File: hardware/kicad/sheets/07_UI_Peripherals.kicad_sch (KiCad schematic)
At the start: 0 parts

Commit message: Implement ESP32-S3 core subsystem
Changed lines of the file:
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@@
-    (effects (font (size 1.27 1.27)) (justify left))
-  )
-  (hierarchical_label "RGB_R_MCU" (shape input) (at 25.4 80.56 0)
-    (effects (font (size 1.27 1.27)) (justify left))
-  )
-  (hierarchical_label "RGB_G_MCU" (shape input) (at 25.4 85.64 0)
-    (effects (font (size 1.27 1.27)) (justify left))
-  )
-  (hierarchical_label "RGB_B_MCU" (shape input) (at 25.4 90.72 0)
-    (effects (font (size 1.27 1.27)) (justify left))
-  )
-  (hierarchical_label "BUZZER_OUT_MCU" (shape input) (at 25.4 95.80 0)
-    (effects (font (size 1.27 1.27)) (justify left))
-  )
-  (hierarchical_label "OLED_RESET_MCU" (shape input) (at 25.4 100.88 0)
     (effects (font (size 1.27 1.27)) (justify left))
   )

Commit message: Implement Package 08 local user interface
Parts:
- added C1: 100 nF X7R ±10% expander reset delay, symbol IPC100:C
- added Q1: 2N7002-class open-drain reset; 100k core pull-up 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, symbol IPC100:OLED_RESET_OD
- added R1: 100 kΩ ±1% expander reset pull-up, symbol IPC100:R
- added R2: 4.70 kΩ ±1% I2C SDA pull-up; Sheet 07 base-bus ow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, symbol IPC100:R
- added R3: 4.70 kΩ ±1% I2C SCL pull-up; Sheet 07 base-bus ow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, symbol IPC100:R
- added TP1: UI_VCC DFT node, symbol IPC100:TEST_NODE
- added TP2: OLED_VCC DFT node, symbol IPC100:TEST_NODE
- added TP3: I2C_SDA DFT node, symbol IPC100:TEST_NODE
- added TP4: I2C_SCL DFT node, symbol IPC100:TEST_NODE
- added TP5: ENCODER_A_COND DFT node, symbol IPC100:TEST_NODE
- added U1: 3ch active-low panel encoder conditioner; 10k/1k/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, symbol IPC100:ENCODER_CONDITIONER3
- added U2: TCA9535-class, +3V3_CORE, address 0x20, power-up 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, symbol IPC100:I2C_EXPANDER
- added U3: 4x 60 V logic NMOS; 100Ω gates; 100kΩ gate pull-d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, symbol IPC100:STATUS_DRIVER4
- added U4: 2.42-inch SSD1309 OLED reference; exact module/J6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, symbol IPC100:I2C_PERIPHERAL_BOUNDARY
- added U5: BME280 environmental sensor reference; exact modu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, symbol IPC100:I2C_PERIPHERAL_BOUNDARY
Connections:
- net +3V3_CORE: now also Q1.1 (RELEASE_CTL), R1.2, R2.2, R3.2, U1.6 (GND), U2.6 (GND)
- net BUZZER_OUT: now also U3.6 (RGB_R)
- net ENCODER_A_COND: now also TP5.1 (NODE), U1.9 (SW_COND)
- net ENCODER_A_RAW: now also U1.4 (B_RAW)
- net ENCODER_B_COND: now also U1.8 (B_COND)
- net ENCODER_B_RAW: now also U1.3 (A_RAW)
- net ENCODER_SW_COND: now also U1.7 (A_COND)
- net ENCODER_SW_RAW: now also U1.2 (UI_VCC)
- net I2C_SCL: now also R3.1, TP4.1 (NODE), U2.5 (ADDR), U4.2 (SDA), U5.2 (SDA)
- net I2C_SDA: now also R2.1, TP3.1 (NODE), U4.3 (SCL), U5.3 (SCL)
- net OLED_RESET: now also Q1.4 (OLED_RESET), U4.1 (VCC)
- net OLED_VCC: now also TP2.1 (NODE), U4.4 (RESET_OR_NC)
- net RGB_B: now also U3.7 (RGB_G)
- net RGB_G: now also U3.8 (RGB_B)
- net RGB_R: now also U3.9 (BUZZER_OUT)
- net SENSOR_VCC: now also U5.4 (RESET_OR_NC)
- net UI_VCC: now also TP1.1 (NODE), U1.5 (SW_RAW)
- new net BUZZER_CTL: U2.8 (RGB_G_CTL), U3.1 (R_CTL)
- new net GND: C1.1, U1.1 (3V3), U2.1 (VCC), U2.3 (SCL)
- new net OLED_RESET_RELEASE: Q1.2 (3V3_DEFAULT_ASSERT), U2.7 (RGB_R_CTL)
- new net RGB_B_CTL: U2.9 (RGB_B_CTL), U3.2 (G_CTL)
- new net RGB_G_CTL: U2.10 (BUZZER_CTL), U3.3 (B_CTL)
- new net RGB_R_CTL: U2.11 (OLED_RESET_RELEASE), U3.4 (BUZ_CTL)
- new net UI_EXPANDER_RESET_N: C1.2, R1.1, U2.4 (RESET_N)
- no-connect marks 0 -> 1
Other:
- note added: "1 — PANEL ENCODER CONDITIONING (ORDINARY UI REQUESTS; NOT SAFETY AUTHORITY)"
- note added: "2 — CORE-POWERED I2C EXPANDER / SAFE-DEFAULT STATUS CONTROL"
- note added: "3 — MAIN-ONLY RGB / BUZZER LOW-SIDE DRIVERS"
- note added: "4 — OLED RESET / DISPLAY & SENSOR I2C BOUNDARIES"
- note added: "5 — SCHEMATIC DFT NODES (PHYSICAL PADS OWNED BY SHEET 09 / PCB DFT)"
- note added: "6 — HIERARCHICAL FUNCTIONAL INTERFACES"
- note added: "Each channel: 10 kΩ UI-domain bias, 1 kΩ series protection, 10 nF filter, Schmitt receiver, low-capacitance ESD provision. UI_VCC invalid forces conditioned output inactive low. Firmware debounce remains required."
- note added: "No ARM/FIRE/STOP, analog adjustment, motor, relay, watchdog, authorization, connector, or raw GPIO circuitry exists on Sheet 07. GPIO37 remains reserved; GPIO42 remains WATCHDOG_SERVICE_MCU on Sheet 03."
- note added: "OLED/SENSOR rails are switched only by Sheet 02 from Sheet 03 requests. Sheet 07 adds no power switch. I2C pull-ups remain core-powered; exact modules must be unpowered-bus safe or receive series isolation in their released interface."
- note added: "Outputs are open-drain current sinks for later Sheet 09 loads. RGB current resistors and final buzzer device remain connector/load dependent; U3 provides only drive, default-OFF bias, and magnetic-load clamp provision."
- note added: "Panel ESD devices and physical connector pinout remain Sheet 09 work. Sheet 07 defines electrical ESD/series/filter requirements only. All component classes and values are preliminary; all footprints remain blank."
- note removed: "Detailed implementation intentionally deferred to subsequent engineering package."
- note removed: "PACKAGE 01 PLACEHOLDER — NO CIRCUITRY OR FOOTPRINTS"
- title: IPC-100 Rev A — 07 UI + OLED + Sensor -> IPC-100 Rev A — 07 User Interface & Local Controls

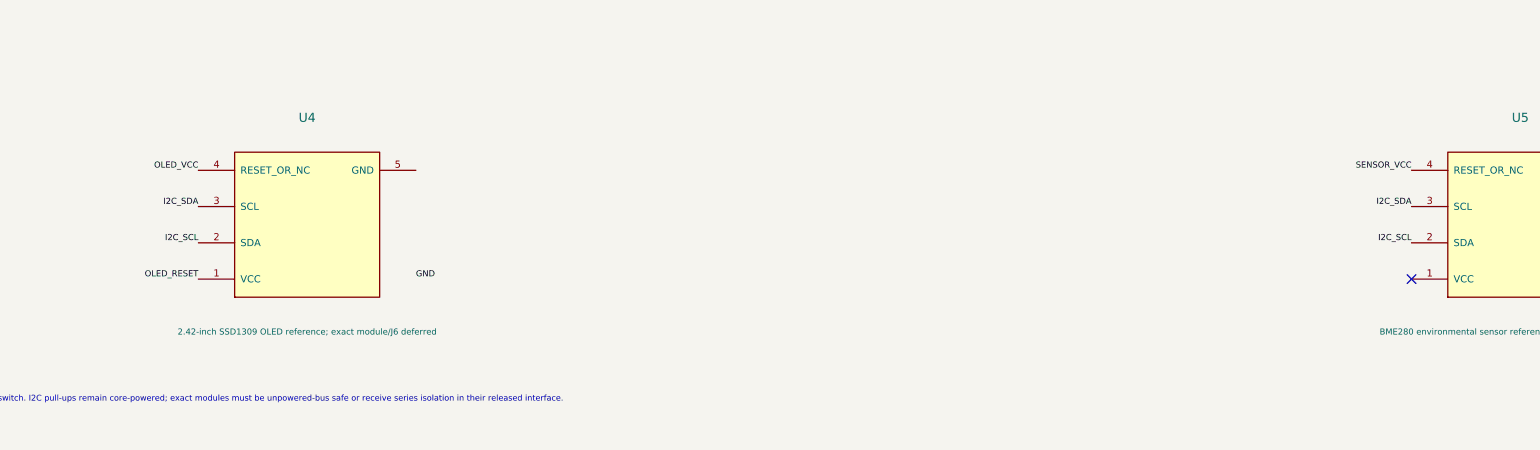
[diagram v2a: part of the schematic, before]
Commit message: Complete ECO-003 hierarchy exposure
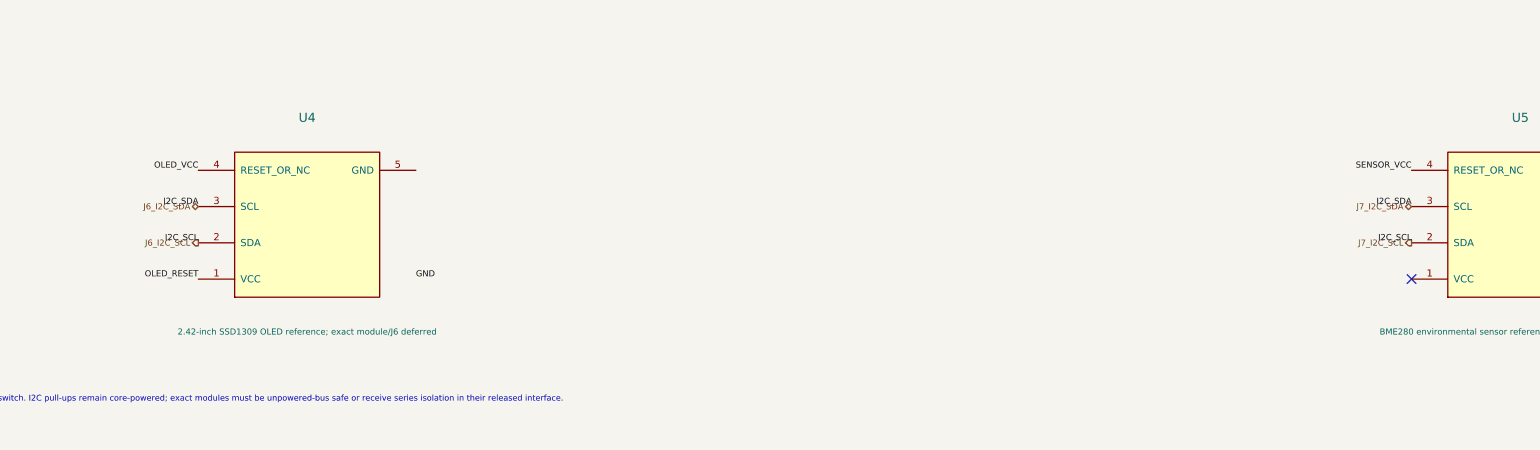
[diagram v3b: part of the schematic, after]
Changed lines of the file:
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@@
   (label "I2C_SDA" (at 104.76 152.46 180) (effects (font (size 0.85 0.85)) (justify right bottom)))
   (label "I2C_SCL" (at 104.76 157.54 180) (effects (font (size 0.85 0.85)) (justify right bottom)))
+  (hierarchical_label "J6_I2C_SDA" (shape bidirectional) (at 104.76 152.46 180) (effects (font (size 0.85 0.85)) (justify right)))
+  (hierarchical_label "J6_I2C_SCL" (shape output) (at 104.76 157.54 180) (effects (font (size 0.85 0.85)) (justify right)))
   (label "OLED_RESET" (at 104.76 162.62 180) (effects (font (size 0.85 0.85)) (justify right bottom)))
   (label "GND" (at 135.24 162.62 0) (effects (font (size 0.85 0.85)) (justify left bottom)))
@@
   (label "I2C_SDA" (at 274.76 152.46 180) (effects (font (size 0.85 0.85)) (justify right bottom)))
   (label "I2C_SCL" (at 274.76 157.54 180) (effects (font (size 0.85 0.85)) (justify right bottom)))
+  (hierarchical_label "J7_I2C_SDA" (shape bidirectional) (at 274.76 152.46 180) (effects (font (size 0.85 0.85)) (justify right)))
+  (hierarchical_label "J7_I2C_SCL" (shape output) (at 274.76 157.54 180) (effects (font (size 0.85 0.85)) (justify right)))
   (no_connect (at 274.76 162.62))
   (label "GND" (at 305.24 162.62 0) (effects (font (size 0.85 0.85)) (justify left bottom)))

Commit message: Complete ECO-004 interface remediation
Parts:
- added U6: J6: 100 kHz; OLED_VCC-qualified; fail-disabled; I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, symbol IPC100:I2C_POWER_QUALIFIED_BRANCH
- added U7: J7: 100 kHz; SENSOR_VCC-qualified; fail-disabled;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, symbol IPC100:I2C_POWER_QUALIFIED_BRANCH
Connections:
- net +3V3_CORE: now also U6.4 (GND), U7.4 (GND)
- net GND: now also U6.1 (BASE_VDD), U6.5 (BRANCH_VDD_QUAL), U7.1 (BASE_VDD), U7.5 (BRANCH_VDD_QUAL)
- net I2C_SCL: now also U6.3 (SCL_BASE), U7.3 (SCL_BASE); no longer U4.2 (SDA), U5.2 (SDA)
- net I2C_SDA: no longer U4.3 (SCL), U5.3 (SCL)
- net OLED_VCC: now also U6.8 (GND)
- net SENSOR_VCC: now also U7.8 (GND)
- new net J6_I2C_SCL: U4.2 (SDA), U6.7 (SCL_BRANCH)
- new net J6_I2C_SDA: U4.3 (SCL)
- new net J7_I2C_SCL: U5.2 (SDA), U7.7 (SCL_BRANCH)
- new net J7_I2C_SDA: U5.3 (SCL)
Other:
- note added: "OLED/SENSOR rails remain Sheet 02 controlled. U6/U7 qualify directly from their own branch rail and isolate before it is invalid. Sheet 07 remains sole owner of the 4.70k base-bus pull-up pair; no branch or Sheet 09 pull-ups."
- note removed: "OLED/SENSOR rails are switched only by Sheet 02 from Sheet 03 requests. Sheet 07 adds no power switch. I2C pull-ups remain core-powered; exact modules must be unpowered-bus safe or receive series isolation in their released interface."
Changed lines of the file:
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@@
   )
   (label "OLED_VCC" (at 104.76 147.38 180) (effects (font (size 0.85 0.85)) (justify right bottom)))
-  (label "I2C_SDA" (at 104.76 152.46 180) (effects (font (size 0.85 0.85)) (justify right bottom)))
-  (label "I2C_SCL" (at 104.76 157.54 180) (effects (font (size 0.85 0.85)) (justify right bottom)))
+  (label "J6_I2C_SDA" (at 104.76 152.46 180) (effects (font (size 0.85 0.85)) (justify right bottom)))
+  (label "J6_I2C_SCL" (at 104.76 157.54 180) (effects (font (size 0.85 0.85)) (justify right bottom)))
   (hierarchical_label "J6_I2C_SDA" (shape bidirectional) (at 104.76 152.46 180) (effects (font (size 0.85 0.85)) (justify right)))
   (hierarchical_label "J6_I2C_SCL" (shape output) (at 104.76 157.54 180) (effects (font (size 0.85 0.85)) (justify right)))
@@
   )
   (label "SENSOR_VCC" (at 274.76 147.38 180) (effects (font (size 0.85 0.85)) (justify right bottom)))
-  (label "I2C_SDA" (at 274.76 152.46 180) (effects (font (size 0.85 0.85)) (justify right bottom)))
-  (label "I2C_SCL" (at 274.76 157.54 180) (effects (font (size 0.85 0.85)) (justify right bottom)))
+  (label "J7_I2C_SDA" (at 274.76 152.46 180) (effects (font (size 0.85 0.85)) (justify right bottom)))
+  (label "J7_I2C_SCL" (at 274.76 157.54 180) (effects (font (size 0.85 0.85)) (justify right bottom)))
   (hierarchical_label "J7_I2C_SDA" (shape bidirectional) (at 274.76 152.46 180) (effects (font (size 0.85 0.85)) (justify right)))
   (hierarchical_label "J7_I2C_SCL" (shape output) (at 274.76 157.54 180) (effects (font (size 0.85 0.85)) (justify right)))
   (no_connect (at 274.76 162.62))
   (label "GND" (at 305.24 162.62 0) (effects (font (size 0.85 0.85)) (justify left bottom)))
-  (text "OLED/SENSOR rails are switched only by Sheet 02 from Sheet 03 requests. Sheet 07 adds no power switch. I2C pull-ups remain core-powered; exact modules must be unpowered-bus safe or receive series isolation in their released interface." (at 20 180 0) (effects (font (size 0.82 0.82)) (justify left bottom)))
+  (symbol (lib_id "IPC100:I2C_POWER_QUALIFIED_BRANCH") (at 380 150 0) (unit 1) (exclude_from_sim no) (in_bom yes) (on_board yes) (dnp no)
+    (property "Reference" "U6" (at 380 133 0) (effects (font (size 1.1 1.1))))
+    (property "Value" "J6: 100 kHz; OLED_VCC-qualified; fail-disabled; Ioff <=10uA; no backfeed/stuck-low propagation while isolated" (at 380 167 0) (effects (font (size 0.72 0.72))))
+    (property "Footprint" "" (at 380 150 0) (effects (font (size 1 1)) hide)) (property "Datasheet" "" (at 380 150 0) (effects (font (size 1 1)) hide))
+    (pin "1") (pin "2") (pin "3") (pin "4") (pin "5") (pin "6") (pin "7") (pin "8")
+    (instances (project "IPC-100" (path "/10000000-0000-4000-8000-000000000001/10000000-0000-4000-8000-000000000365" (reference "U6") (unit 1))))
+  )
+  (label "+3V3_CORE" (at 362.22 139.84 180) (effects (font (size .72 .72)) (justify right bottom)))
+  (label "I2C_SDA" (at 362.22 144.92 180) (effects (font (size .72 .72)) (justify right bottom)))
+  (label "I2C_SCL" (at 362.22 150 180) (effects (font (size .72 .72)) (justify right bottom)))
+  (label "GND" (at 362.22 160.16 180) (effects (font (size .72 .72)) (justify right bottom)))
+  (label "OLED_VCC" (at 397.78 139.84 0) (effects (font (size .72 .72)) (justify left bottom)))
+  (label "J6_I2C_SDA" (at 397.78 144.92 0) (effects (font (size .72 .72)) (justify left bottom)))
+  (label "J6_I2C_SCL" (at 397.78 150 0) (effects (font (size .72 .72)) (justify left bottom)))
+  (label "GND" (at 397.78 160.16 0) (effects (font (size .72 .72)) (justify left bottom)))
+  (symbol (lib_id "IPC100:I2C_POWER_QUALIFIED_BRANCH") (at 475 150 0) (unit 1) (exclude_from_sim no) (in_bom yes) (on_board yes) (dnp no)
+    (property "Reference" "U7" (at 475 133 0) (effects (font (size 1.1 1.1))))
+    (property "Value" "J7: 100 kHz; SENSOR_VCC-qualified; fail-disabled; Ioff <=10uA; no backfeed/stuck-low propagation while isolated" (at 475 167 0) (effects (font (size 0.72 0.72))))
+    (property "Footprint" "" (at 475 150 0) (effects (font (size 1 1)) hide)) (property "Datasheet" "" (at 475 150 0) (effects (font (size 1 1)) hide))
+    (pin "1") (pin "2") (pin "3") (pin "4") (pin "5") (pin "6") (pin "7") (pin "8")
+    (instances (project "IPC-100" (path "/10000000-0000-4000-8000-000000000001/10000000-0000-4000-8000-000000000365" (reference "U7") (unit 1))))
+  )
+  (label "+3V3_CORE" (at 457.22 139.84 180) (effects (font (size .72 .72)) (justify right bottom)))
+  (label "I2C_SDA" (at 457.22 144.92 180) (effects (font (size .72 .72)) (justify right bottom)))
+  (label "I2C_SCL" (at 457.22 150 180) (effects (font (size .72 .72)) (justify right bottom)))
+  (label "GND" (at 457.22 160.16 180) (effects (font (size .72 .72)) (justify right bottom)))
+  (label "SENSOR_VCC" (at 492.78 139.84 0) (effects (font (size .72 .72)) (justify left bottom)))
+  (label "J7_I2C_SDA" (at 492.78 144.92 0) (effects (font (size .72 .72)) (justify left bottom)))
+  (label "J7_I2C_SCL" (at 492.78 150 0) (effects (font (size .72 .72)) (justify left bottom)))
+  (label "GND" (at 492.78 160.16 0) (effects (font (size .72 .72)) (justify left bottom)))
+  (text "OLED/SENSOR rails remain Sheet 02 controlled. U6/U7 qualify directly from their own branch rail and isolate before it is invalid. Sheet 07 remains sole owner of the 4.70k base-bus pull-up pair; no branch or Sheet 09 pull-ups." (at 20 180 0) (effects (font (size 0.82 0.82)) (justify left bottom)))
   (text "5 — SCHEMATIC DFT NODES (PHYSICAL PADS OWNED BY SHEET 09 / PCB DFT)" (at 20 200 0) (effects (font (size 1.15 1.15) (bold yes)) (justify left bottom)))
   (symbol (lib_id "IPC100:TEST_NODE") (at 80 215 0) (unit 1) (exclude_from_sim no) (in_bom no) (on_board no) (dnp no)

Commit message: Normalize Rev A reference designators
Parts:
- renumbered C1 to C701, Q1 to Q701, R1 to R701, R2 to R702, R3 to R703, TP1 to TP701, TP2 to TP702, TP3 to TP703, TP4 to TP704, TP5 to TP705, U1 to U701, U2 to U702, U3 to U703, U4 to U704, U5 to U705, U6 to U706, U7 to U707
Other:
- note added: "OLED/SENSOR rails remain Sheet 02 controlled. U706/U707 qualify directly from their own branch rail and isolate before it is invalid. Sheet 07 remains sole owner of the 4.70k base-bus pull-up pair; no branch or Sheet 09 pull-ups."
- note removed: "OLED/SENSOR rails remain Sheet 02 controlled. U6/U7 qualify directly from their own branch rail and isolate before it is invalid. Sheet 07 remains sole owner of the 4.70k base-bus pull-up pair; no branch or Sheet 09 pull-ups."
